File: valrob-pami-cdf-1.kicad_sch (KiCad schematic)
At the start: 79 parts, among them J1 Conn_01x04, J10 Conn_01x04_Pin, J3 USB_C_Receptacle_USB2.0_14P, M1 Motor_Servo, Q1 Q_NMOS, Q2 Q_NMOS, SW1 SW_SPST, SW3 SW_Push, SW4 SW_Push, U1 BQ77905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

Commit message: schem: import buzzer
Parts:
- added BZ1: Buzzer, GLCS:MagneticBuzzer_Huaneng_MLT-5020, symbol Device:Buzzer
- added Q3: Q_NMOS, Package_TO_SOT_SMD:SOT-323_SC-70, symbol Device:Q_NMOS
- added R18: 510, Resistor_SMD:R_0402_1005Metric, symbol Device:R
- added TP3: TestPoint, TestPoint:TestPoint_Pad_D2.0mm, symbol Connector:TestPoint
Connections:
- net +3V3: now also BZ1.1 (+)
- net GND: now also Q3.2 (S)
- new net: BZ1.2 (-), Q3.3 (D), TP3.1
- new net: Q3.1 (G), R18.2
- new net BUZZER: R18.1
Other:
- note added: "Buzzer"

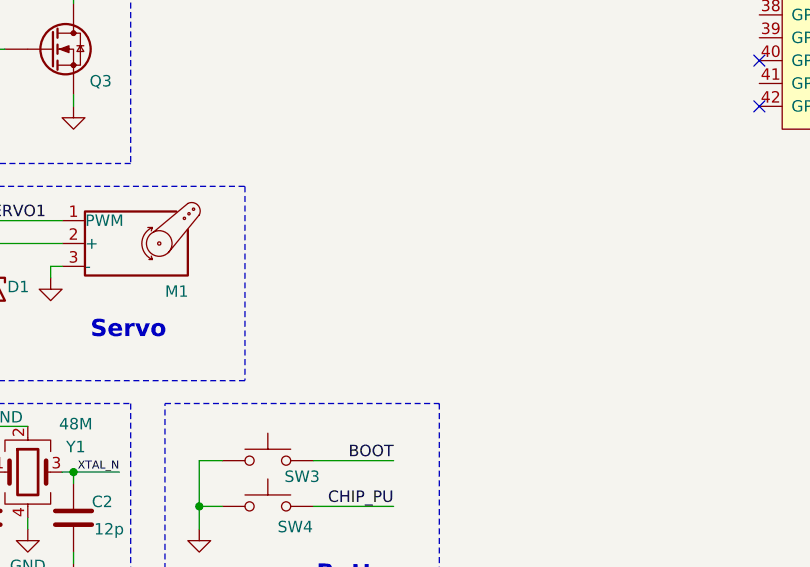
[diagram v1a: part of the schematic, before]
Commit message: schem: add XT30 battery connector
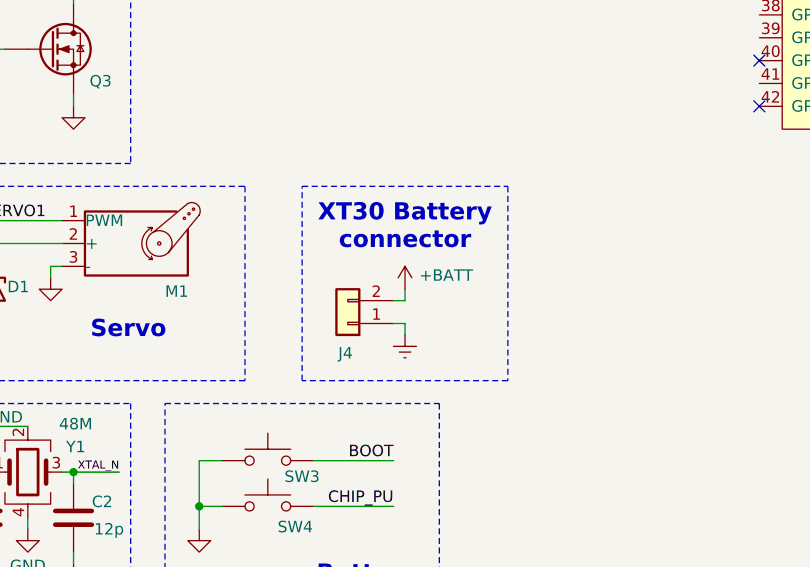
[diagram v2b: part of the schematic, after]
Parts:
- added J4: Conn_01x02, Connector_AMASS:AMASS_XT30U-M_1x02_P5.0mm_Vertical, symbol Connector_Generic:Conn_01x02
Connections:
- net +BATT: now also J4.2 (Pin_2)
- net BGND: now also J4.1 (Pin_1)
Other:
- note added: "XT30 Battery connector"

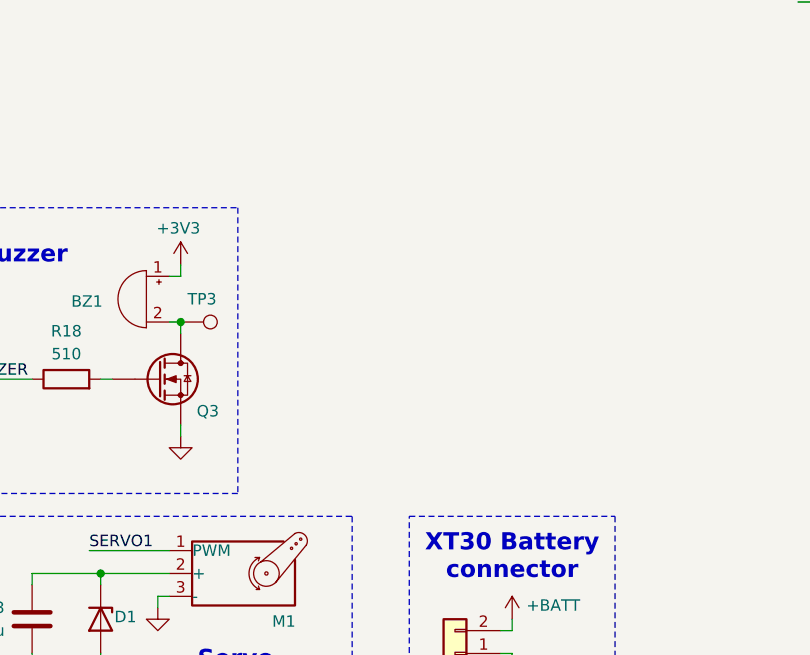
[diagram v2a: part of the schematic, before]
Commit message: pcb: add indicator leds
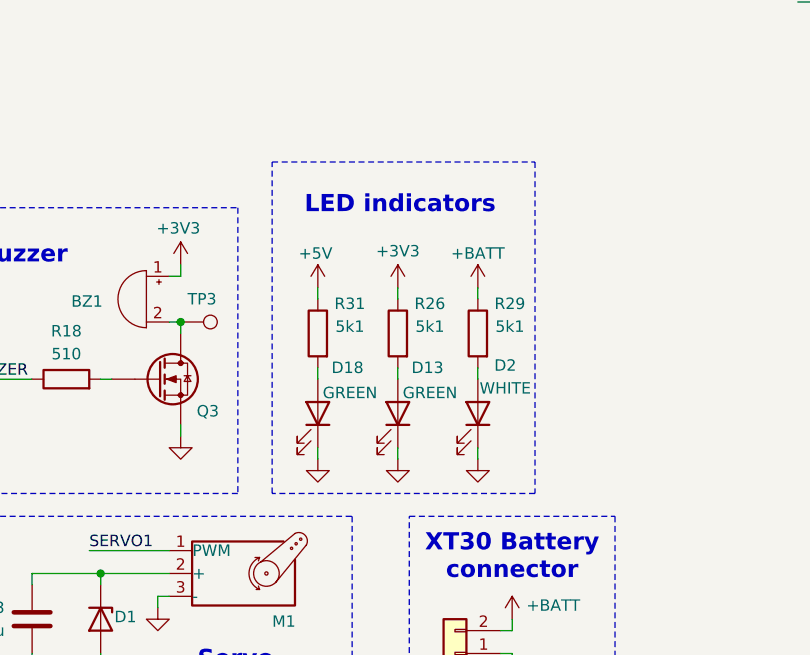
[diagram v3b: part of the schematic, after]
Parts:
- added D13, D18: GREEN, LED_SMD:LED_0805_2012Metric, symbol Device:LED
- added D2: WHITE, LED_SMD:LED_0603_1608Metric, symbol Device:LED
- added R26, R29, R31: 5k1, Resistor_SMD:R_0402_1005Metric, symbol Device:R
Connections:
- net +3V3: now also R26.1
- net +5V: now also R31.1
- net +BATT: now also R29.1
- net GND: now also D13.1 (K), D18.1 (K), D2.1 (K)
- new net: D13.2 (A), R26.2
- new net: D18.2 (A), R31.2
- new net: D2.2 (A), R29.2
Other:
- note added: "LED indicators"

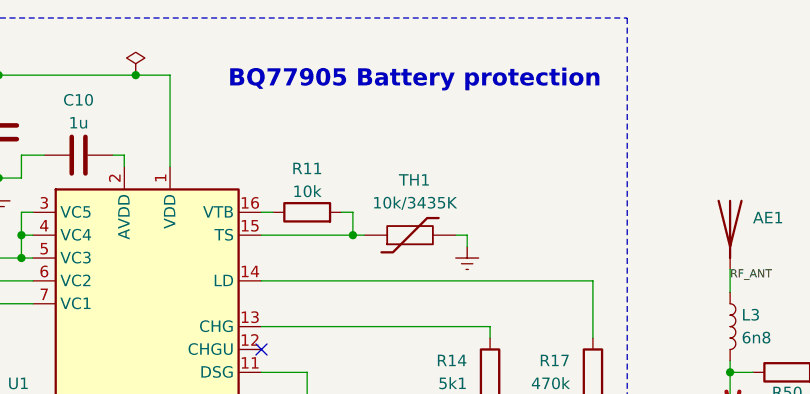
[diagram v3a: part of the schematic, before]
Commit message: schem: add BQ77905 enable pull down resistor
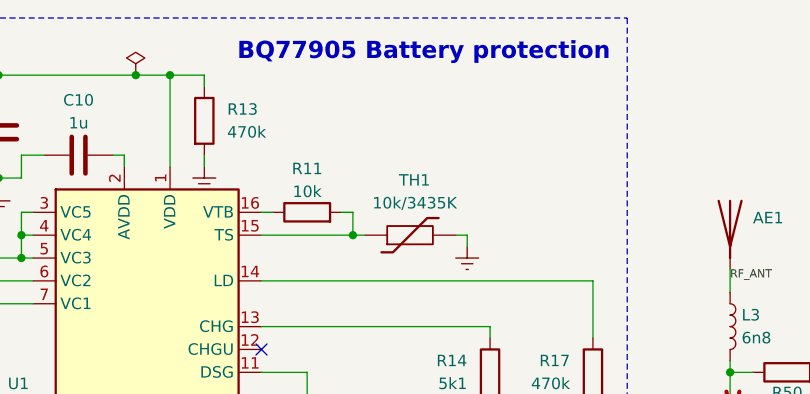
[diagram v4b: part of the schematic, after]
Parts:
- added R13: 470k, Resistor_SMD:R_0603_1608Metric, symbol Device:R
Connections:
- net BGND: now also R13.2
- net at C8.2, R7.2, U1.1 (VDD): now also R13.1
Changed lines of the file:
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@@
 	(text "BQ77905 Battery protection"
 		(exclude_from_sim no)
-		(at 107.188 25.908 0)
+		(at 108.204 22.86 0)
 		(effects
 			(font
@@
 	)
 	(junction
+		(at 80.01 25.4)
+		(diameter 0)
+		(color 0 0 0 0)
+	)
+	(junction
 		(at 204.47 34.29)
 		(diameter 0)
@@
 	(wire
 		(pts
+			(xy 83.82 34.29) (xy 83.82 35.56)
+		)
+		(stroke
+			(width 0)
+			(type default)
+		)
+	)
+	(wire
+		(pts
 			(xy 88.9 83.82) (xy 88.9 85.09)
 		)
@@
 	(wire
 		(pts
+			(xy 83.82 26.67) (xy 83.82 25.4)
+		)
+		(stroke
+			(width 0)
+			(type default)
+		)
+	)
+	(wire
+		(pts
 			(xy 34.29 24.13) (xy 34.29 25.4)
 		)
@@
 	(wire
 		(pts
+			(xy 83.82 25.4) (xy 80.01 25.4)
+		)
+		(stroke
+			(width 0)
+			(type default)
+		)
+	)
+	(wire
+		(pts
 			(xy 43.18 179.07) (xy 60.96 179.07)
 		)
@@
 	)
 	(symbol
+		(lib_id "Device:R")
+		(at 83.82 30.48 0)
+		(unit 1)
+		(exclude_from_sim no)
+		(in_bom yes)
+		(on_board yes)
+		(dnp no)
+		(property "Reference" "R13"
+			(at 86.36 29.2099 0)
+			(effects
+				(font
+					(size 1.27 1.27)
+				)
+				(justify left)
+			)
+		)
+		(property "Value" "470k"
+			(at 86.36 31.7499 0)
+			(effects
+				(font
+					(size 1.27 1.27)
+				)
+				(justify left)
+			)
+		)
+		(property "Footprint" "Resistor_SMD:R_0603_1608Metric"
+			(at 82.042 30.48 90)
+			(effects
+				(font
+					(size 1.27 1.27)
+				)
+				(hide yes)
+			)
+		)
+		(property "Datasheet" "~"
+			(at 83.82 30.48 0)
+			(effects
+				(font
+					(size 1.27 1.27)
+				)
+				(hide yes)
+			)
+		)
+		(property "Description" "Resistor"
+			(at 83.82 30.48 0)
+			(effects
+				(font
+					(size 1.27 1.27)
+				)
+				(hide yes)
+			)
+		)
+		(property "Basic" "Y"
+			(at 83.82 30.48 0)
+			(effects
+				(font
+					(size 1.27 1.27)
+				)
+				(hide yes)
+			)
+		)
+		(property "JLCPCB Part #" "C23178"
+			(at 83.82 30.48 0)
+			(effects
+				(font
+					(size 1.27 1.27)
+				)
+				(hide yes)
+			)
+		)
+		(property "Manufacturer" "Uniroyal Elec"
+			(at 83.82 30.48 0)
+			(effects
+				(font
+					(size 1.27 1.27)
+				)
+				(hide yes)
+			)
+		)
+		(property "Manufacturer Part Number" "0603WAF4703T5E"
+			(at 83.82 30.48 0)
+			(effects
+				(font
+					(size 1.27 1.27)
+				)
+				(hide yes)
+			)
+		)
+		(pin "2"
+		)
+		(pin "1"
+		)
+		(instances
+			(project "valrob-pami-cdf-1"
+				(path "/453def7e-2a78-4c3c-a4b7-f12883e5bdd2"
+					(reference "R13")
+					(unit 1)
+				)
+			)
+		)
+	)
+	(symbol
 		(lib_id "power:GND")
 		(at 119.38 187.96 0)
@@
 					(unit 1)
 				)
+			)
+		)
+	)
+	(symbol
+		(lib_id "power:Earth")
+		(at 83.82 35.56 0)
+		(unit 1)
+		(exclude_from_sim no)
+		(in_bom yes)
+		(on_board yes)
+		(dnp no)
+		(property "Reference" "#PWR07"
+			(at 83.82 41.91 0)
+			(effects
+				(font
+					(size 1.27 1.27)
+				)
+				(hide yes)
+			)
+		)
+		(property "Value" "BGND"
+			(at 83.82 39.624 0)
+			(effects
+				(font
+					(size 1.27 1.27)
+				)
+				(hide yes)
+			)
+		)
+		(property "Footprint" ""
+			(at 83.82 35.56 0)
+			(effects
+				(font
+					(size 1.27 1.27)
+				)
+				(hide yes)
+			)
+		)
+		(property "Datasheet" "~"
+			(at 83.82 35.56 0)
+			(effects
+				(font
+					(size 1.27 1.27)
+				)
+				(hide yes)
+			)
+		)
+		(property "Description" "Power symbol creates a global label with name \"Earth\""
+			(at 83.82 35.56 0)
+			(effects
+				(font
+					(size 1.27 1.27)
+				)
+				(hide yes)
+			)
+		)
+		(pin "1"
+		)
+		(instances
+			(project "valrob-pami-cdf-1"
+				(path "/453def7e-2a78-4c3c-a4b7-f12883e5bdd2"
+					(reference "#PWR07")
+					(unit 1)
+				)

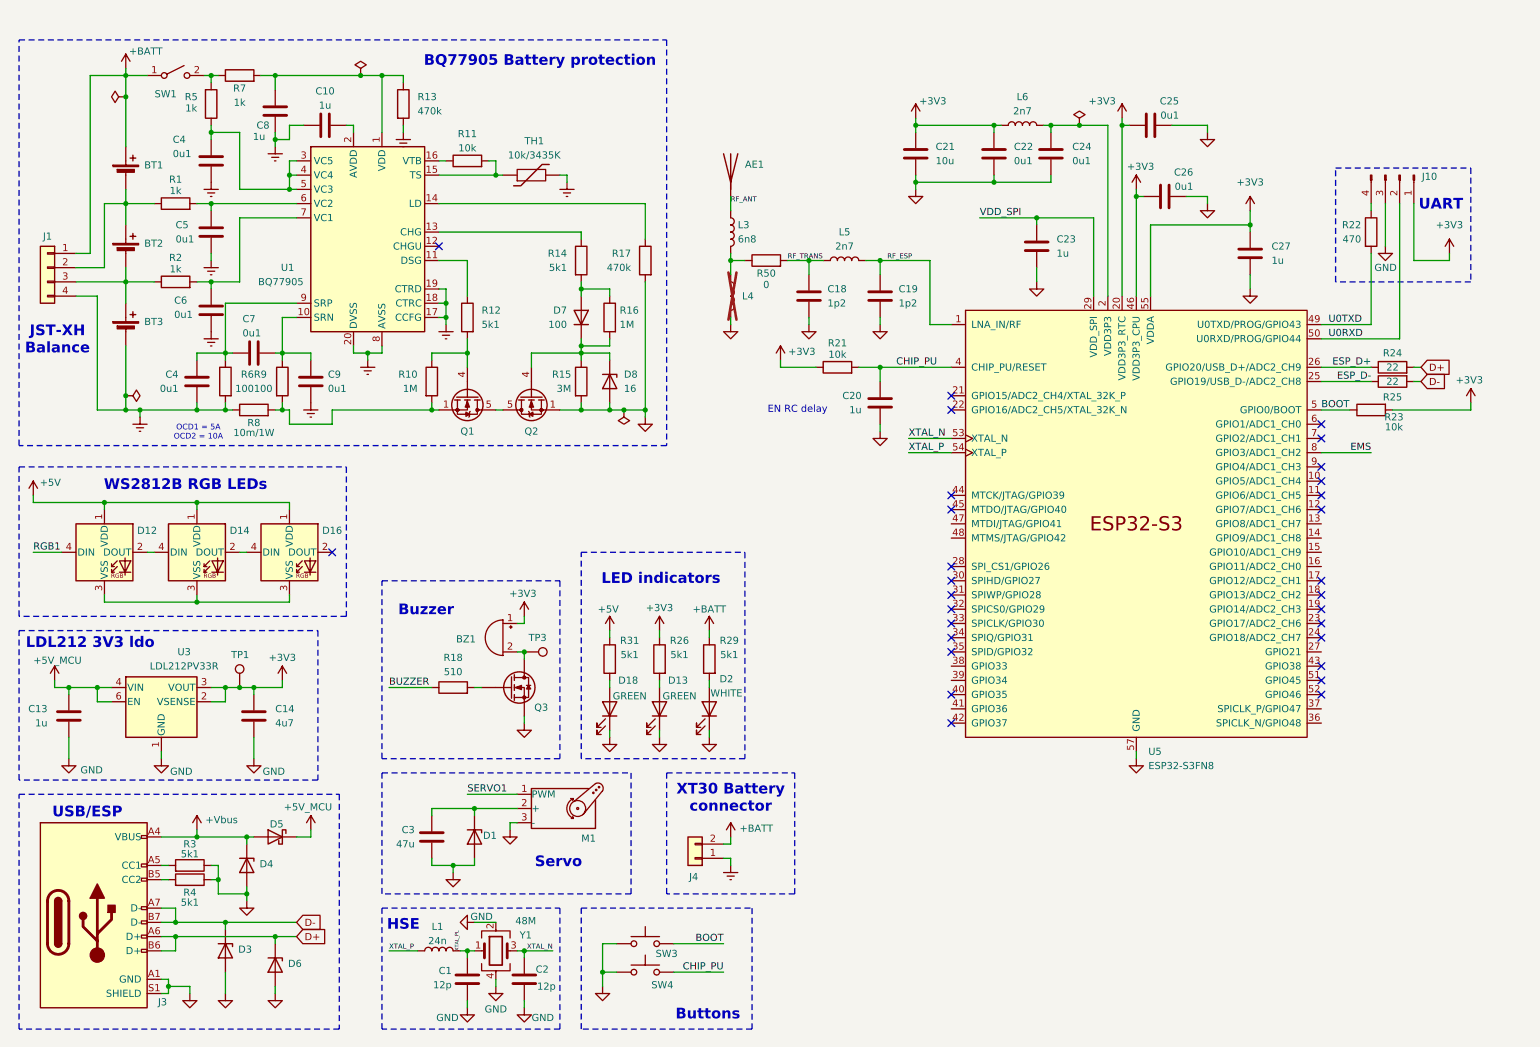
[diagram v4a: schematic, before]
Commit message: schem: import DRV8424 stepper driver and reorganize
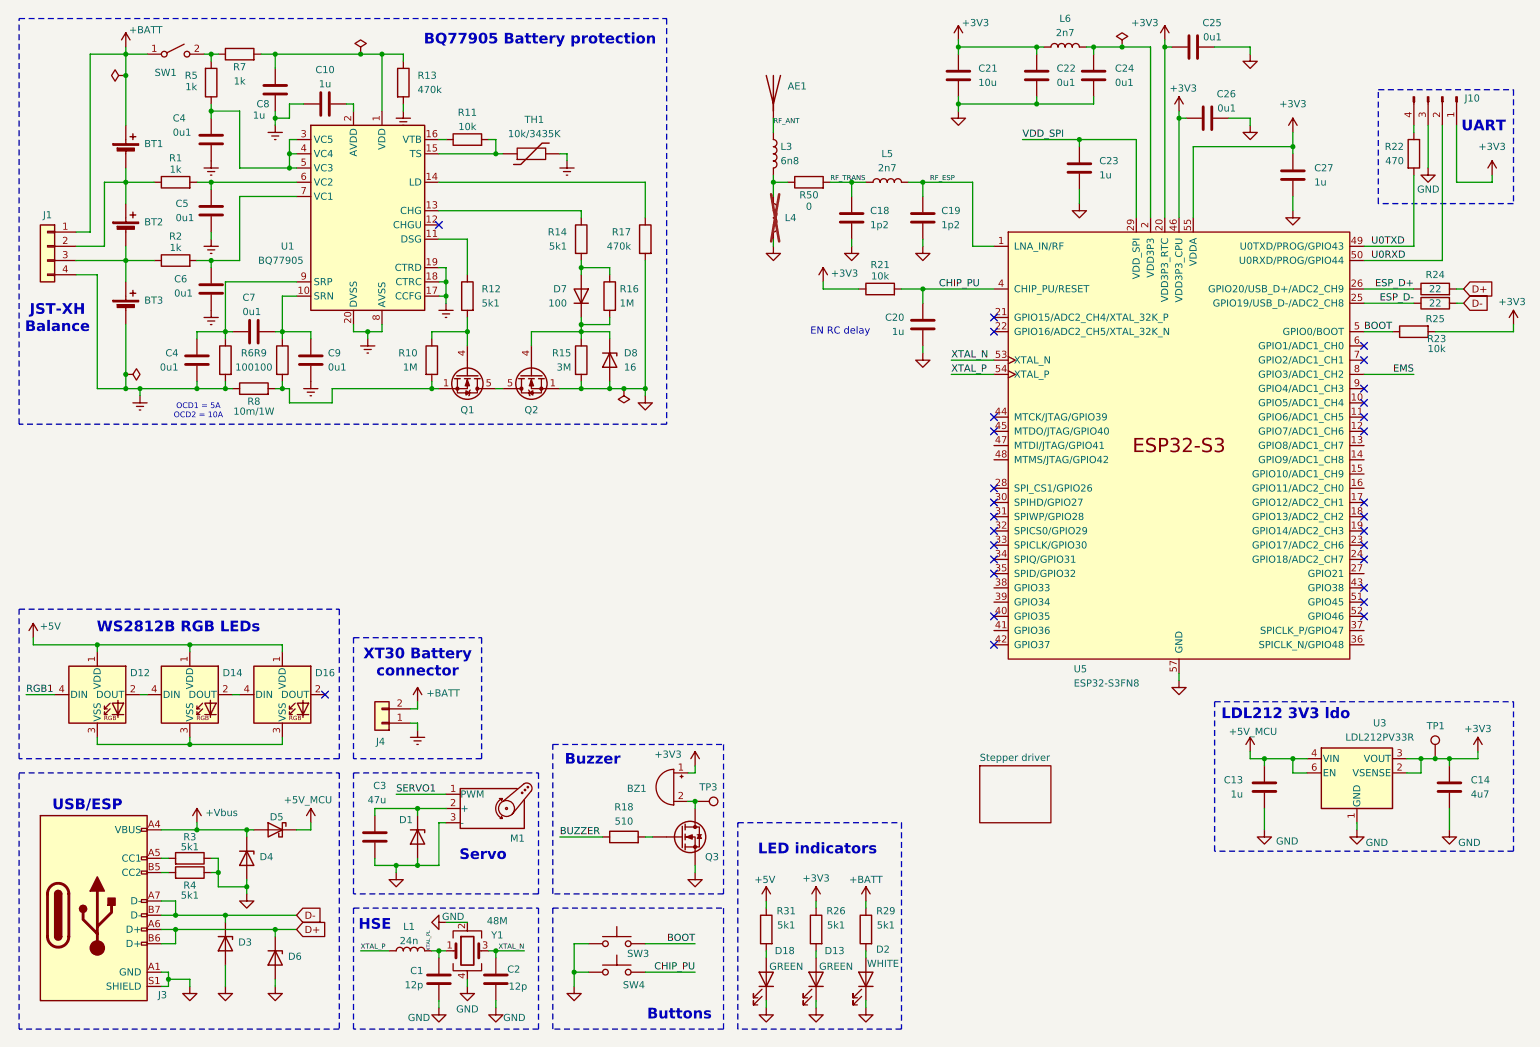
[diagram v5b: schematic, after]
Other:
- added sheet Stepper driver (stepper.kicad_sch)
- moved on the sheet: AE1, BT1, BT2, BT3, BZ1, C1, C10, C13, C14, C18, C19, C2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

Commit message: schem: add placeholder TPS56A37 5V smps
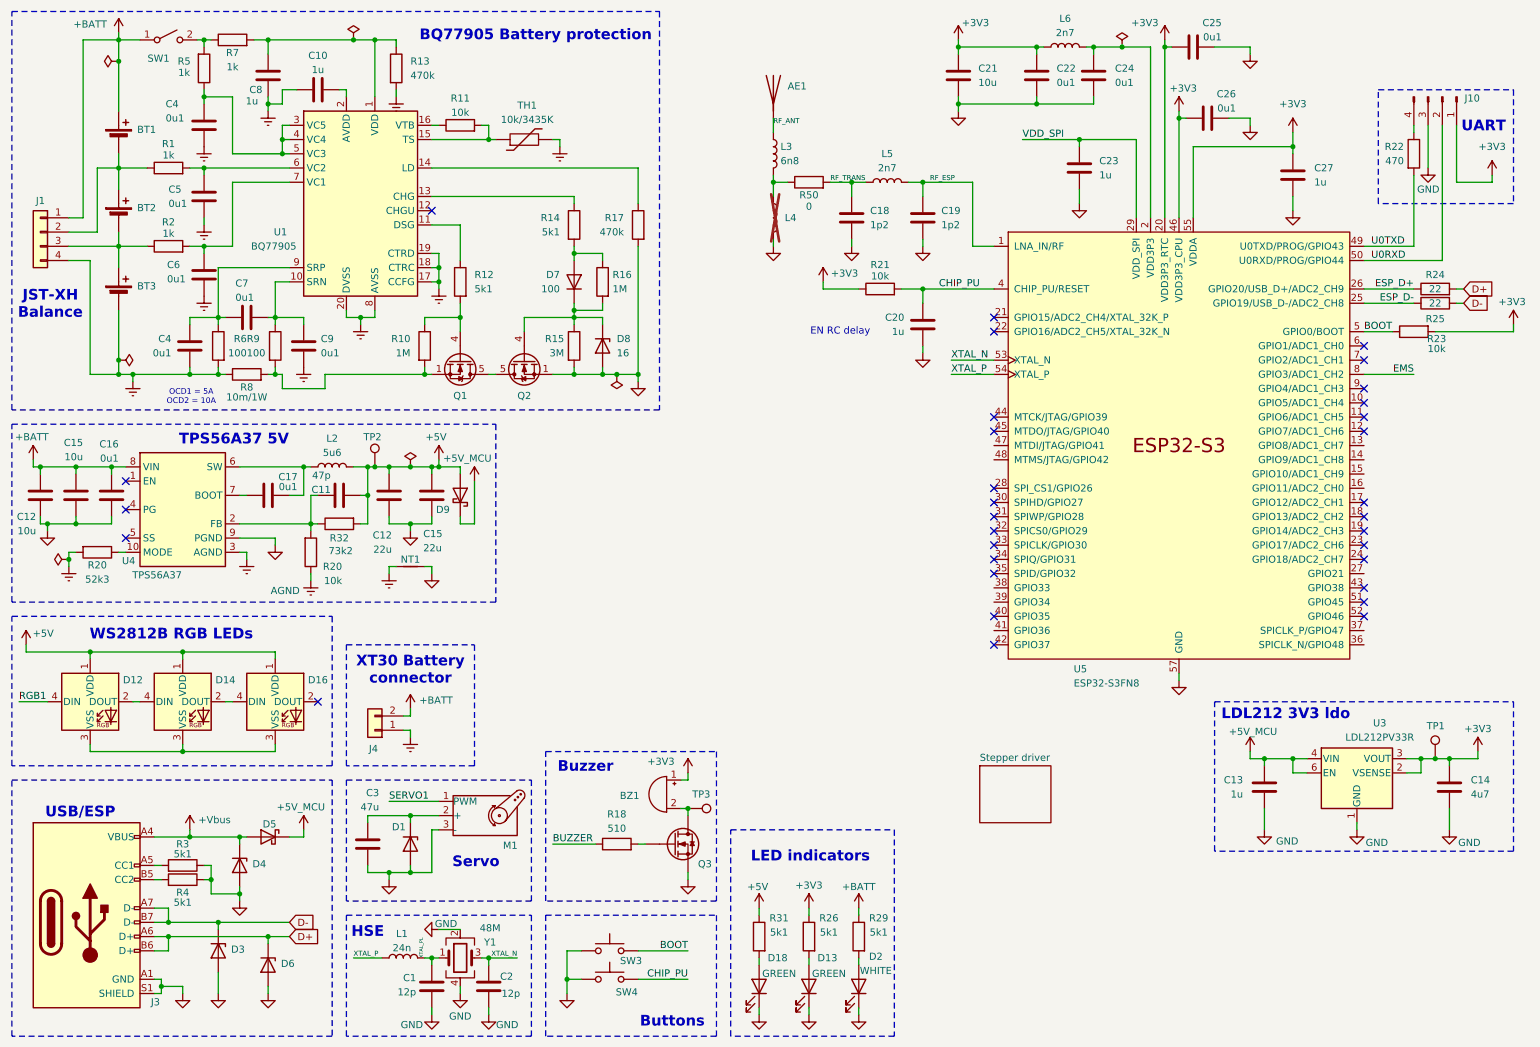
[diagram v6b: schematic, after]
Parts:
- added C11: 47p, Capacitor_SMD:C_0402_1005Metric, symbol Device:C
- added C12, C15: 22u, Capacitor_SMD:C_0805_2012Metric, symbol Device:C
- added C12, C15: 10u, Capacitor_SMD:C_0805_2012Metric, symbol Device:C
- added C16, C17: 0u1, Capacitor_SMD:C_0402_1005Metric, symbol Device:C
- added D9: D_Schottky, Diode_SMD:D_SMA, symbol Device:D_Schottky
- added L2: 5u6, Inductor_SMD:L_10.4x10.4_H4.8, symbol Device:L
- added NT1: NetTie_2, NetTie:NetTie-2_SMD_Pad0.5mm, symbol Device:NetTie_2
- added R20: 10k, Resistor_SMD:R_0402_1005Metric, symbol Device:R
- added R20: 52k3, Resistor_SMD:R_0402_1005Metric, symbol Device:R
- added R32: 73k2, Resistor_SMD:R_0402_1005Metric, symbol Device:R
- added TP2: TestPoint, TestPoint:TestPoint_Pad_D2.0mm, symbol Connector:TestPoint
- added U4: TPS56A37, GLCS:Texas_RPA0010A_VQFN-HR-10_3x3mm_P0.5mm, symbol GLCS:TPS56A37
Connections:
- net +5V: now also C11.2, C12.1, C15.1, D9.2 (A), L2.2, R32.2, TP2.1
- net +5V_MCU: now also D9.1 (K)
- net +BATT: now also C12.1, C15.1, C16.1, U4.8 (VIN)
- net GND: now also C12.2, C12.2, C15.2, C15.2, C16.2, NT1.2, U4.9 (PGND)
- new net: C11.1, R20.2, R32.1, U4.2 (FB)
- new net: C17.2, L2.1, U4.6 (SW)
- new net: R20.1, U4.10 (MODE)
- new net: C17.1, U4.7 (BOOT)
- new net AGND: NT1.1, R20.1, R20.2, U4.3 (AGND)
- no-connect marks 29 -> 32
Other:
- note added: "TPS56A37 5V"
- moved on the sheet: BT1, BT2, BT3, BZ1, C1, C10, C2, C3, C4, C5, C6, C7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
